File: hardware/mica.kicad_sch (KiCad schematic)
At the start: 29 parts

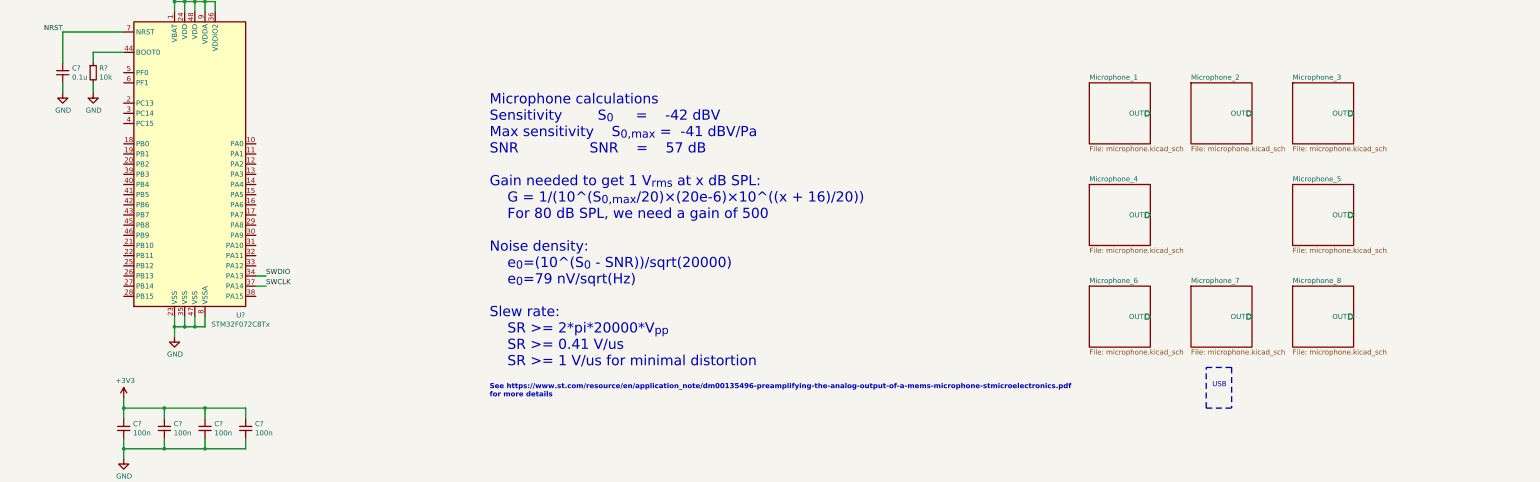
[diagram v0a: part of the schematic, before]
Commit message: Simulate amplification circuit and adjust values accordingly
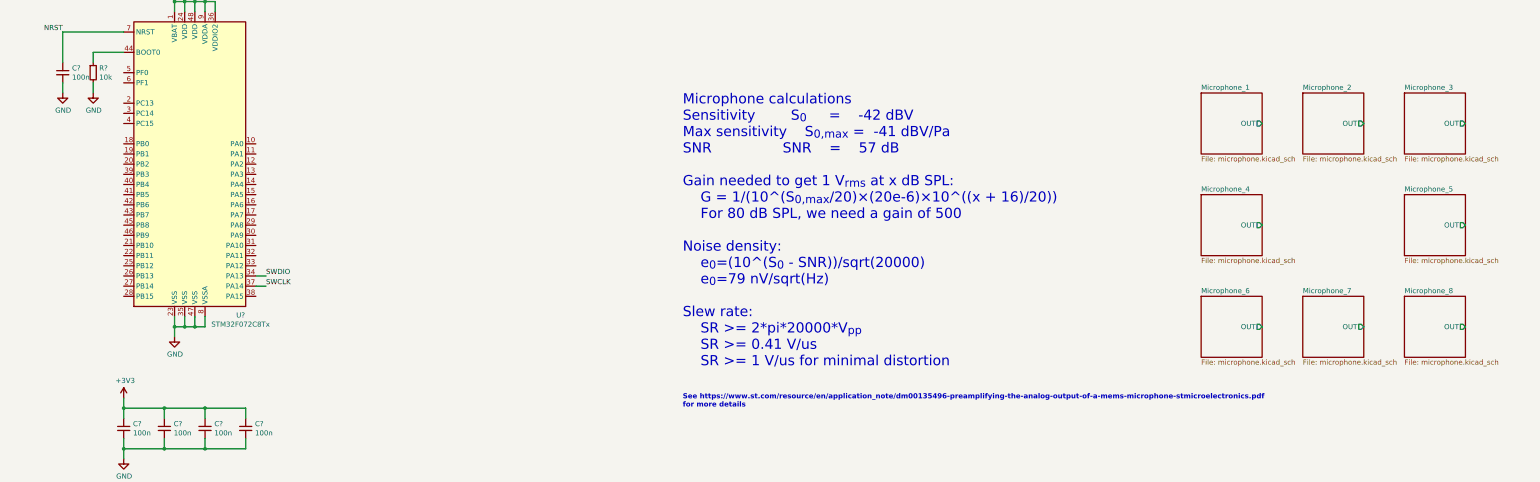
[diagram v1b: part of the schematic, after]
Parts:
- C? (x7): Dielectric (none) -> -; Tolerance (none) -> 10%; Voltage (none) -> 6.3V
- C?: value 0.1u -> 100n; Dielectric (none) -> -; Tolerance (none) -> 10%; Voltage (none) -> 6.3V
- R? (x5): Tolerance (none) -> 1%; Voltage (none) -> 50V
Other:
- note removed: "USB"

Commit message: Cleanup schematic, connect usb
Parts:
- gave numbers to parts that had none: 29
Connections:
- net USB_D+: now also U1.33 (PA12)
- net USB_D-: now also U1.32 (PA11)
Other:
- note added: "3.3V regulator"
- note added: "Decoupling"
- note added: "Microcontroller"
- note added: "Microphone array"
- note added: "Mounting"
- note added: "SWD programming"
- note added: "USB connector"
- note added: "User interface"
- note removed: "Microphone calculations Sensitivity S_{0} = -42 dBV Max sensitivity S_{0,max} = -41 dBV/Pa SNR SNR = 57 dB Gain needed to get 1 V_{rms} at x dB SPL: G = 1/(10^(S_{0,max}/20)×(20e-6)×10^((x + 16)/20)) For 80 dB SPL, we need a gain of 500 Noise density: e_{0}=(10^(S_{0} - SNR))/sqrt(20000) e_{0}=79 nV/sqrt(Hz) Slew rate: SR >= 2*pi*20000*V_{pp} SR >= 0.41 V/us SR >= 1 V/us for minimal distortion"
- note removed: "See https://www.st.com/resource/en/application_note/dm00135496-preamplifying-the-analog-output-of-a-mems-microphone-stmicroelectronics.pdf for more details"
- moved on the sheet: C1, C2, C3, C4, C5, C6, C7, C8, D1, D2, F1, J1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
